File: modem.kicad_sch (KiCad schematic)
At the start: 17 parts, among them J1 1775862-2, J4 Pins_2.54_1x2, J5 Pins_2.54_1x2, M5 MM60-EZH039-B5-R850, Q1 2N7002-7-F, U4 AP22804AW5-7

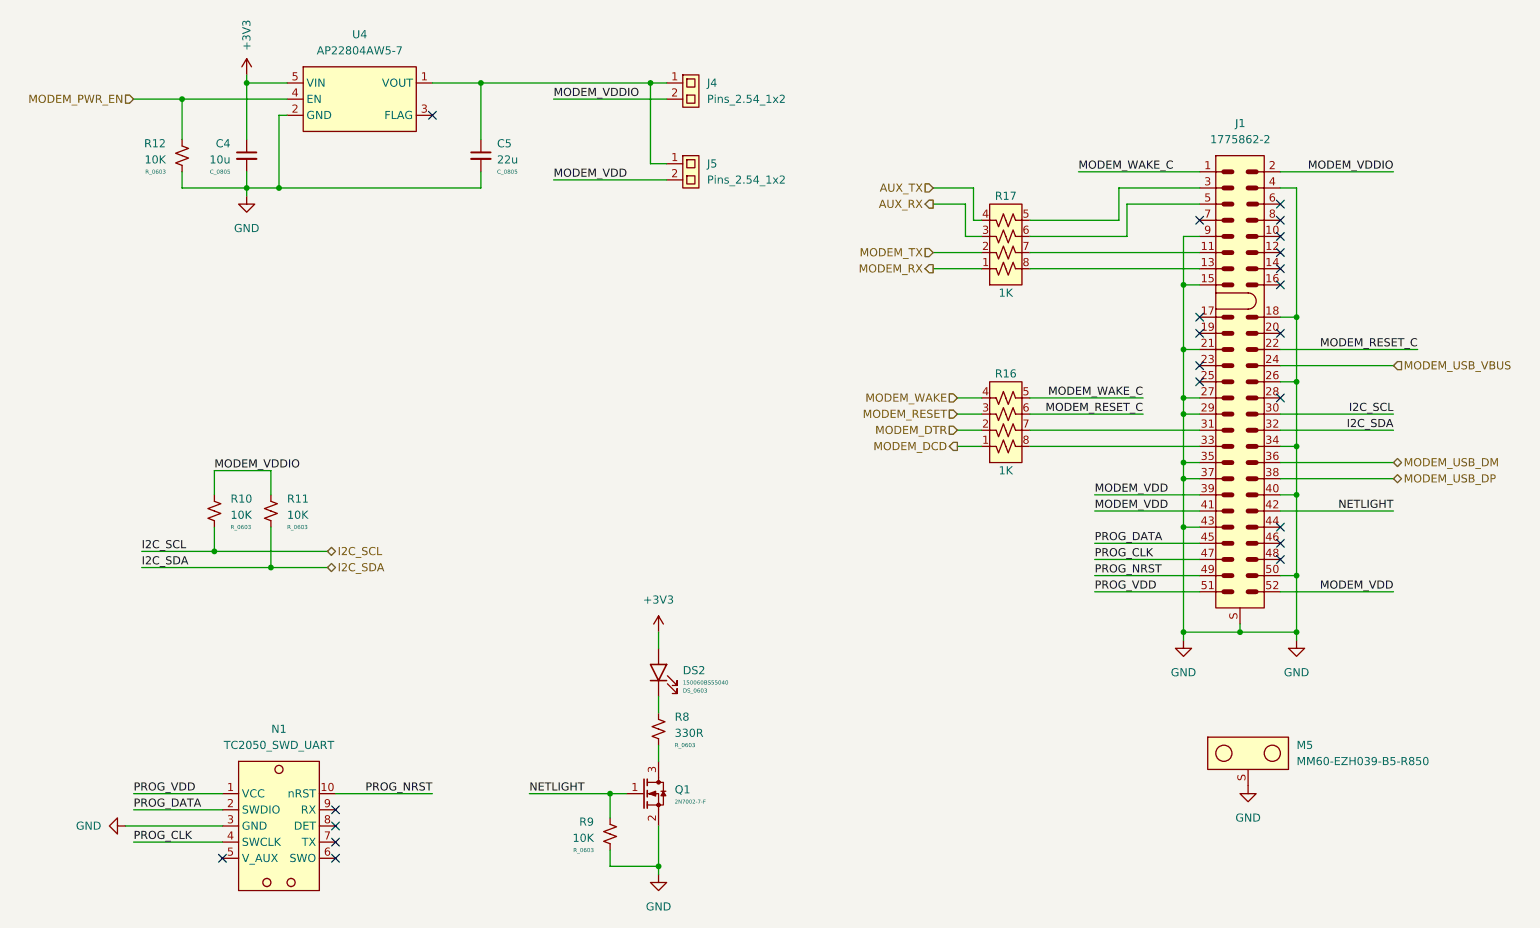
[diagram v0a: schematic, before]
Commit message: Reannotate components
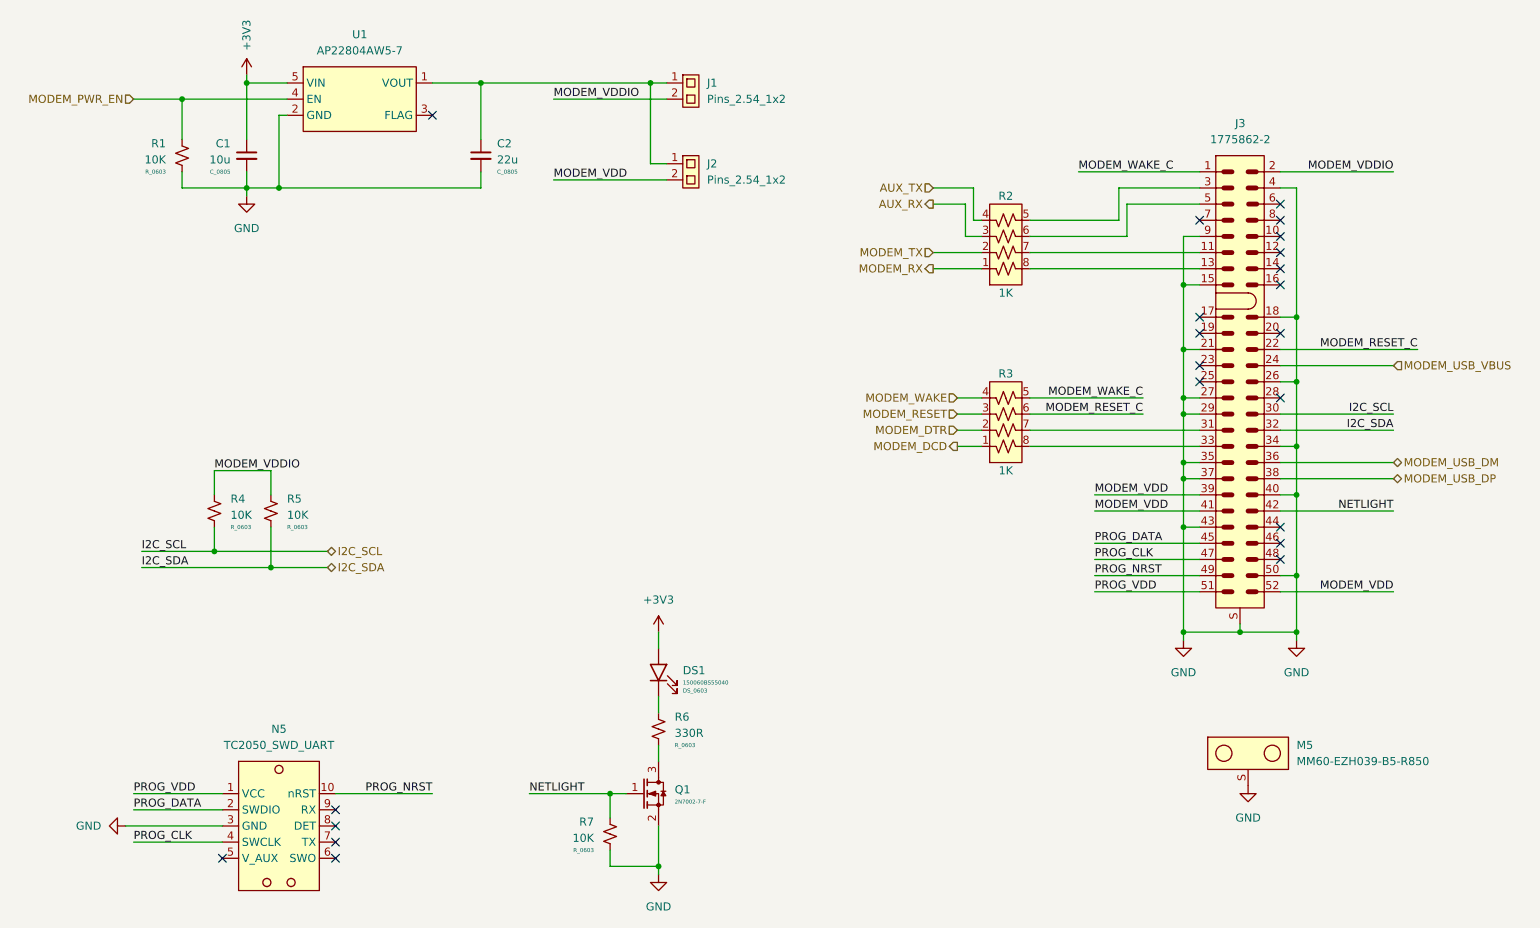
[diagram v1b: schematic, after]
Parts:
- renumbered C4 to C1, C5 to C2, DS2 to DS1, J4 to J1, J5 to J2, J1 to J3, N1 to N5, R12 to R1, R17 to R2, R16 to R3, R10 to R4, R11 to R5, R8 to R6, R9 to R7, U4 to U1
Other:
- company: (none) -> TL Embedded
- title: (none) -> Winglet Carrier Board
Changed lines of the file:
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@@
 	(generator_version "8.0")
 	(paper "A4")
+	(title_block
+		(title "Winglet Carrier Board")
+		(date "2024-08-09")
+		(rev "v1.0")
+		(company "TL Embedded")
+	)
 	(junction
 		(at 128.27 35.56)
@@
 		(dnp no)
 		(fields_autoplaced yes)
-		(property "Reference" "R8"
+		(property "Reference" "R6"
 			(at 132.08 135.2549 0)
 			(effects
@@
 			(project ""
 				(path "/bbb905ef-a222-43ea-83e2-d1132f7d94bb/660a82c3-3048-4bd7-90de-0f4f117d8c92"
-					(reference "R8")
+					(reference "R6")
 					(unit 1)
 				)
@@
 		(dnp no)
 		(fields_autoplaced yes)
-		(property "Reference" "#PWR027"
+		(property "Reference" "#PWR08"
 			(at 129.54 166.37 0)
 			(effects
@@
 			(project "Winglet-Carrier"
 				(path "/bbb905ef-a222-43ea-83e2-d1132f7d94bb/660a82c3-3048-4bd7-90de-0f4f117d8c92"
-					(reference "#PWR027")
+					(reference "#PWR08")
 					(unit 1)
 				)
@@
 		(dnp no)
 		(fields_autoplaced yes)
-		(property "Reference" "#PWR06"
+		(property "Reference" "#PWR04"
 			(at 212.09 129.54 0)
 			(effects
@@
 			(project "Winglet-Carrier"
 				(path "/bbb905ef-a222-43ea-83e2-d1132f7d94bb/660a82c3-3048-4bd7-90de-0f4f117d8c92"
-					(reference "#PWR06")
+					(reference "#PWR04")
 					(unit 1)
 				)
@@
 		(on_board yes)
 		(dnp no)
-		(property "Reference" "J4"
+		(property "Reference" "J1"
 			(at 137.16 35.5599 0)
 			(effects
@@
 			(project "Winglet-Carrier"
 				(path "/bbb905ef-a222-43ea-83e2-d1132f7d94bb/660a82c3-3048-4bd7-90de-0f4f117d8c92"
-					(reference "J4")
+					(reference "J1")
 					(unit 1)
 				)
@@
 		(on_board yes)
 		(dnp no)
-		(property "Reference" "#PWR028"
+		(property "Reference" "#PWR03"
 			(at 129.54 125.73 0)
 			(effects
@@
 			(project ""
 				(path "/bbb905ef-a222-43ea-83e2-d1132f7d94bb/660a82c3-3048-4bd7-90de-0f4f117d8c92"
-					(reference "#PWR028")
+					(reference "#PWR03")
 					(unit 1)
 				)
@@
 		(dnp no)
 		(fields_autoplaced yes)
-		(property "Reference" "#PWR03"
+		(property "Reference" "#PWR02"
 			(at 64.77 59.69 0)
 			(effects
@@
 			(project "Winglet-Carrier"
 				(path "/bbb905ef-a222-43ea-83e2-d1132f7d94bb/660a82c3-3048-4bd7-90de-0f4f117d8c92"
-					(reference "#PWR03")
+					(reference "#PWR02")
 					(unit 1)
 				)
@@
 		(dnp no)
 		(fields_autoplaced yes)
-		(property "Reference" "U4"
+		(property "Reference" "U1"
 			(at 82.55 27.94 0)
 			(effects
@@
 			(project ""
 				(path "/bbb905ef-a222-43ea-83e2-d1132f7d94bb/660a82c3-3048-4bd7-90de-0f4f117d8c92"
-					(reference "U4")
+					(reference "U1")
 					(unit 1)
 				)
@@
 		(dnp no)
 		(fields_autoplaced yes)
-		(property "Reference" "DS2"
+		(property "Reference" "DS1"
 			(at 133.35 127.9524 90)
 			(effects
@@
 			(project ""
 				(path "/bbb905ef-a222-43ea-83e2-d1132f7d94bb/660a82c3-3048-4bd7-90de-0f4f117d8c92"
-					(reference "DS2")
+					(reference "DS1")
 					(unit 1)
 				)
@@
 		(dnp no)
 		(fields_autoplaced yes)
-		(property "Reference" "R11"
+		(property "Reference" "R5"
 			(at 71.12 100.9649 0)
 			(effects
@@
 			(project "Winglet-Carrier"
 				(path "/bbb905ef-a222-43ea-83e2-d1132f7d94bb/660a82c3-3048-4bd7-90de-0f4f117d8c92"
-					(reference "R11")
+					(reference "R5")
 					(unit 1)
 				)
@@
 		(dnp no)
 		(fields_autoplaced yes)
-		(property "Reference" "C5"
+		(property "Reference" "C2"
 			(at 104.14 45.0912 0)
 			(effects
@@
 			(project "Winglet-Carrier"
 				(path "/bbb905ef-a222-43ea-83e2-d1132f7d94bb/660a82c3-3048-4bd7-90de-0f4f117d8c92"
-					(reference "C5")
+					(reference "C2")
 					(unit 1)
 				)
@@
 		(on_board yes)
 		(dnp no)
-		(property "Reference" "#PWR04"
+		(property "Reference" "#PWR01"
 			(at 64.77 38.1 0)
 			(effects
@@
 			(project "Winglet-Carrier"
 				(path "/bbb905ef-a222-43ea-83e2-d1132f7d94bb/660a82c3-3048-4bd7-90de-0f4f117d8c92"
-					(reference "#PWR04")
+					(reference "#PWR01")
 					(unit 1)
 				)
@@
 		(dnp no)
 		(fields_autoplaced yes)
-		(property "Reference" "R12"
+		(property "Reference" "R1"
 			(at 52.07 45.0849 0)
 			(effects
@@
 			(project "Winglet-Carrier"
 				(path "/bbb905ef-a222-43ea-83e2-d1132f7d94bb/660a82c3-3048-4bd7-90de-0f4f117d8c92"
-					(reference "R12")
+					(reference "R1")
 					(unit 1)
 				)
@@
 		(on_board yes)
 		(dnp no)
-		(property "Reference" "J5"
+		(property "Reference" "J2"
 			(at 137.16 48.2599 0)
 			(effects
@@
 			(project "Winglet-Carrier"
 				(path "/bbb905ef-a222-43ea-83e2-d1132f7d94bb/660a82c3-3048-4bd7-90de-0f4f117d8c92"
-					(reference "J5")
+					(reference "J2")
 					(unit 1)
 				)
@@
 		(dnp no)
 		(fields_autoplaced yes)
-		(property "Reference" "R9"
+		(property "Reference" "R7"
 			(at 119.38 151.7649 0)
 			(effects
@@
 			(project "Winglet-Carrier"
 				(path "/bbb905ef-a222-43ea-83e2-d1132f7d94bb/660a82c3-3048-4bd7-90de-0f4f117d8c92"
-					(reference "R9")
+					(reference "R7")
 					(unit 1)
 				)
@@
 		(dnp no)
 		(fields_autoplaced yes)
-		(property "Reference" "R10"
+		(property "Reference" "R4"
 			(at 62.23 100.9649 0)
 			(effects
@@
 			(project "Winglet-Carrier"
 				(path "/bbb905ef-a222-43ea-83e2-d1132f7d94bb/660a82c3-3048-4bd7-90de-0f4f117d8c92"
-					(reference "R10")
+					(reference "R4")
 					(unit 1)
 				)
@@
 		(on_board yes)
 		(dnp no)
-		(property "Reference" "R16"
+		(property "Reference" "R3"
 			(at 184.15 81.28 0)
 			(effects
@@
 			(project "Winglet-Carrier"
 				(path "/bbb905ef-a222-43ea-83e2-d1132f7d94bb/660a82c3-3048-4bd7-90de-0f4f117d8c92"
-					(reference "R16")
+					(reference "R3")
 					(unit 1)
 				)
@@
 		(dnp no)
 		(fields_autoplaced yes)
-		(property "Reference" "J1"
+		(property "Reference" "J3"
 			(at 221.0221 41.91 0)
 			(effects
@@
 			(project "Winglet-Carrier"
 				(path "/bbb905ef-a222-43ea-83e2-d1132f7d94bb/660a82c3-3048-4bd7-90de-0f4f117d8c92"
-					(reference "J1")
+					(reference "J3")
 					(unit 1)
 				)
@@
 		(on_board yes)
 		(dnp no)
-		(property "Reference" "C4"
+		(property "Reference" "C1"
 			(at 62.23 45.0912 0)
 			(effects
@@
 			(project "Winglet-Carrier"
 				(path "/bbb905ef-a222-43ea-83e2-d1132f7d94bb/660a82c3-3048-4bd7-90de-0f4f117d8c92"
-					(reference "C4")
+					(reference "C1")
 					(unit 1)
 				)
@@
 		(dnp no)
 		(fields_autoplaced yes)
-		(property "Reference" "#PWR08"
+		(property "Reference" "#PWR07"
 			(at 39.37 152.4 0)
 			(effects
@@
 			(project "Winglet-Carrier"
 				(path "/bbb905ef-a222-43ea-83e2-d1132f7d94bb/660a82c3-3048-4bd7-90de-0f4f117d8c92"
-					(reference "#PWR08")
+					(reference "#PWR07")
 					(unit 1)
 				)
@@
 		(dnp no)
 		(fields_autoplaced yes)
-		(property "Reference" "#PWR032"
+		(property "Reference" "#PWR06"
 			(at 222.25 152.4 0)
 			(effects
@@
 			(project "Winglet-Carrier"
 				(path "/bbb905ef-a222-43ea-83e2-d1132f7d94bb/660a82c3-3048-4bd7-90de-0f4f117d8c92"
-					(reference "#PWR032")
+					(reference "#PWR06")
 					(unit 1)
 				)
@@
 		(on_board yes)
 		(dnp no)
-		(property "Reference" "R17"
+		(property "Reference" "R2"
 			(at 184.15 53.34 0)
 			(effects
@@
 			(project "Winglet-Carrier"
 				(path "/bbb905ef-a222-43ea-83e2-d1132f7d94bb/660a82c3-3048-4bd7-90de-0f4f117d8c92"
-					(reference "R17")
+					(reference "R2")
 					(unit 1)
 				)
@@
 		(dnp no)
 		(fields_autoplaced yes)
-		(property "Reference" "N1"
+		(property "Reference" "N5"
 			(at 69.85 137.16 0)
 			(effects
@@
 			(project "Winglet-Carrier"
 				(path "/bbb905ef-a222-43ea-83e2-d1132f7d94bb/660a82c3-3048-4bd7-90de-0f4f117d8c92"
-					(reference "N1")
+					(reference "N5")
 					(unit 1)
 				)
